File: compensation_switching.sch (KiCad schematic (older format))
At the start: 5 parts, among them U16 TMUX6111PWR

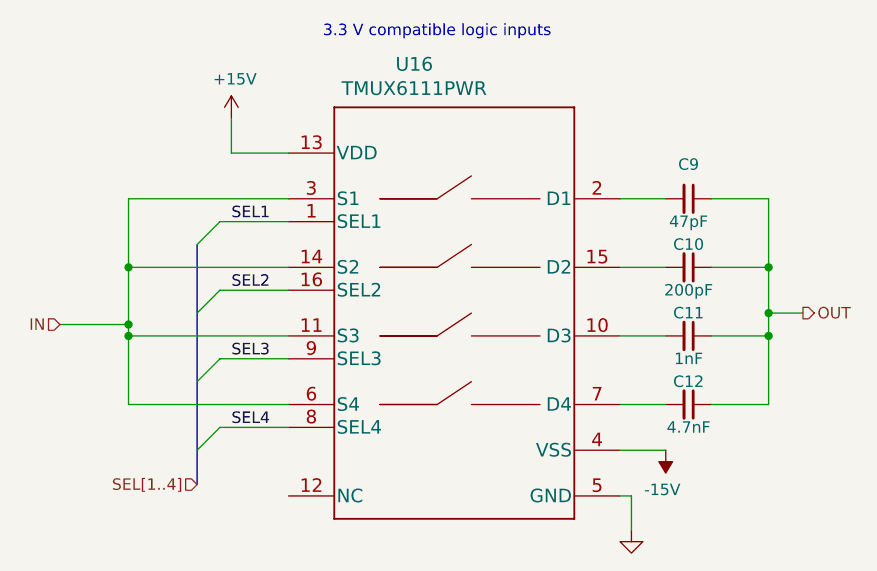
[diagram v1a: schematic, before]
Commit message: reduced ERC to just 4 warnings
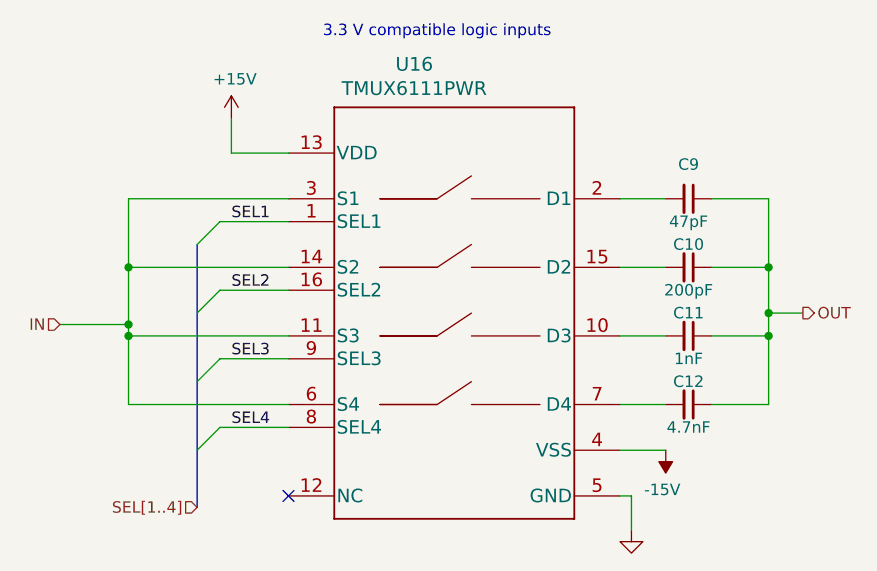
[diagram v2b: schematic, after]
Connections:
- no-connect marks 0 -> 1
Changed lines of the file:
@@
 $Descr A4 11693 8268
 encoding utf-8
-Sheet 3 6
+Sheet 6 6
 Title ""
 Date ""
@@
 AR Path="/6032F251/60DEADCD/60E82840" Ref="C?"  Part="1"
 AR Path="/6032F251/60DEBB32/60E82840" Ref="C?"  Part="1"
+AR Path="/6032F251/6217F546/60E82840" Ref="C9"  Part="1"
 F 0 "C9" V 6450 3300 50  0000 C CNN
 F 1 "47pF" V 6700 3300 50  0000 C CNN
@@
 AR Path="/6032F251/60DEADCD/60E839D5" Ref="C?"  Part="1"
 AR Path="/6032F251/60DEBB32/60E839D5" Ref="C?"  Part="1"
+AR Path="/6032F251/6217F546/60E839D5" Ref="C10"  Part="1"
 F 0 "C10" V 6500 3600 50  0000 C CNN
 F 1 "200pF" V 6700 3600 50  0000 C CNN
@@
 AR Path="/6032F251/60DEADCD/60E83CD7" Ref="C?"  Part="1"
 AR Path="/6032F251/60DEBB32/60E83CD7" Ref="C?"  Part="1"
+AR Path="/6032F251/6217F546/60E83CD7" Ref="C11"  Part="1"
 F 0 "C11" V 6500 3900 50  0000 C CNN
 F 1 "1nF" V 6700 3900 50  0000 C CNN
@@
 AR Path="/6032F251/60DEADCD/60E84E8C" Ref="C?"  Part="1"
 AR Path="/6032F251/60DEBB32/60E84E8C" Ref="C?"  Part="1"
+AR Path="/6032F251/6217F546/60E84E8C" Ref="C12"  Part="1"
 F 0 "C12" V 6500 4200 50  0000 C CNN
 F 1 "4.7nF" V 6700 4200 50  0000 C CNN
@@
 AR Path="/6032F251/60DEADCD/60EA6FEC" Ref="#PWR?"  Part="1"
 AR Path="/6032F251/60DEBB32/60EA6FEC" Ref="#PWR?"  Part="1"
+AR Path="/6032F251/6217F546/60EA6FEC" Ref="#PWR048"  Part="1"
 F 0 "#PWR048" H 6500 4500 50  0001 C CNN
 F 1 "-15V" H 6515 4573 50  0000 C CNN
@@
 AR Path="/6032F251/60DEADCD/60EA7501" Ref="#PWR?"  Part="1"
 AR Path="/6032F251/60DEBB32/60EA7501" Ref="#PWR?"  Part="1"
+AR Path="/6032F251/6217F546/60EA7501" Ref="#PWR046"  Part="1"
 F 0 "#PWR046" H 4600 2800 50  0001 C CNN
 F 1 "+15V" H 4615 3123 50  0000 C CNN
@@
 AR Path="/6032F251/60DEADCD/60EA8BF4" Ref="#PWR?"  Part="1"
 AR Path="/6032F251/60DEBB32/60EA8BF4" Ref="#PWR?"  Part="1"
+AR Path="/6032F251/6217F546/60EA8BF4" Ref="#PWR047"  Part="1"
 F 0 "#PWR047" H 6350 4500 50  0001 C CNN
 F 1 "GND" H 6355 4577 50  0001 C CNN
@@
 AR Path="/6032F251/60DEADCD/60E9BE9C" Ref="U?"  Part="1"
 AR Path="/6032F251/60DEBB32/60E9BE9C" Ref="U?"  Part="1"
+AR Path="/6032F251/6217F546/60E9BE9C" Ref="U16"  Part="1"
 F 0 "U16" H 5400 4888 60  0000 C CNN
 F 1 "TMUX6111PWR" H 5400 4782 60  0000 C CNN
@@
 	1    0    0    -1
 $EndComp
-Text HLabel 4450 4550 0    50   Input ~ 0
+Text HLabel 4450 4650 0    50   Input ~ 0
 SEL[1..4]
 Text HLabel 3850 3850 0    50   Input ~ 0
@@
 Connection ~ 4150 3850
 Connection ~ 6950 3800
+NoConn ~ 4850 4600
 Wire Bus Line
-	4450 3500 4450 4550
+	4450 3500 4450 4650
 $EndSCHEMATC

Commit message: updates to pcb layout
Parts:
- U16: footprint digikey-footprints:TSSOP-14_W4.4mm -> Package_SO:TSSOP-16_4.4x5mm_P0.65mm
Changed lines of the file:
@@
 F 0 "U16" H 5400 4888 60  0000 C CNN
 F 1 "TMUX6111PWR" H 5400 4782 60  0000 C CNN
-F 2 "digikey-footprints:TSSOP-14_W4.4mm" H 5400 3740 60  0001 C CNN
+F 2 "Package_SO:TSSOP-16_4.4x5mm_P0.65mm" H 5400 3740 60  0001 C CNN
 F 3 "" H 5400 3800 60  0001 C CNN
 F 4 "TMUX6111PWR" H 5400 3800 50  0001 C CNN "Manf#"

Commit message: updates to schematic for alternate part #s
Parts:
- C12: Alternative MPN CL10C332JB8NNNC -> (none); Alternative Manf# (none) -> CL10C332JB8NNNC
- U16: Alternate Manf# (none) -> TMUX6112PWR; Alternate2 Manf# (none) -> TMUX6113PWR
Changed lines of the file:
@@
 F 2 "Capacitor_SMD:C_0603_1608Metric" H 6638 4050 50  0001 C CNN
 F 3 "~" H 6600 4200 50  0001 C CNN
-F 4 "CL10C332JB8NNNC" H 6500 4200 50  0001 C CNN "Alternative MPN"
-F 5 "CC0603JRNPO9BN332" H 6500 4200 50  0001 C CNN "Manf#"
+F 4 "CC0603JRNPO9BN332" H 6500 4200 50  0001 C CNN "Manf#"
+F 5 "CL10C332JB8NNNC" H 6500 4200 50  0001 C CNN "Alternative Manf#"
 F 6 "5%" H 6500 4200 50  0001 C CNN "Tolerance"
 F 7 "50V" H 6500 4200 50  0001 C CNN "voltage"
@@
 F 3 "" H 5400 3800 60  0001 C CNN
 F 4 "TMUX6111PWR" H 5400 3800 50  0001 C CNN "Manf#"
+F 5 "TMUX6112PWR" H 5400 3800 50  0001 C CNN "Alternate Manf#"
+F 6 "TMUX6113PWR" H 5400 3800 50  0001 C CNN "Alternate2 Manf#"
 	1    5400 3800
 	1    0    0    -1

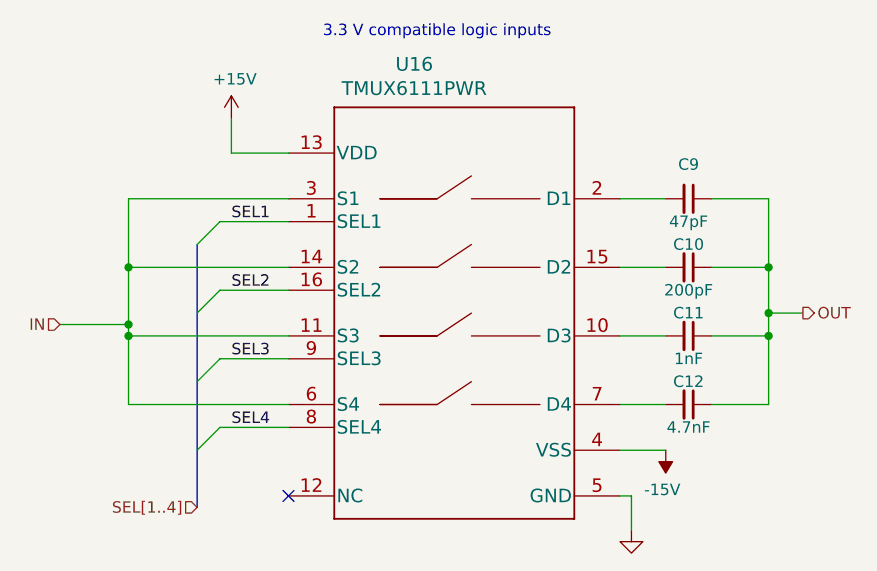
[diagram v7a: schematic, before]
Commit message: nearly completed layout re-route
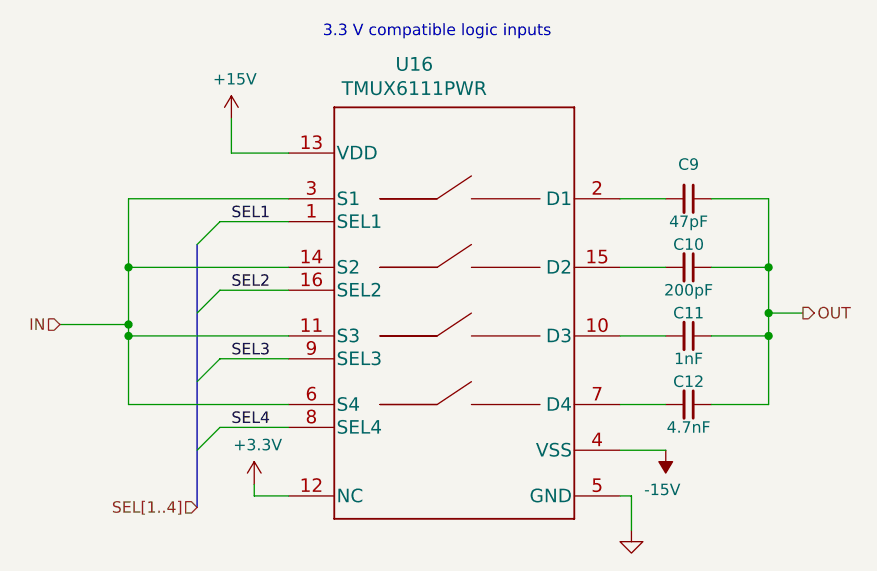
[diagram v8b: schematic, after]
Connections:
- net +3V3: now reaches U16.12 (NC)
- no-connect marks 1 -> 0
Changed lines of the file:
@@
 Connection ~ 4150 3850
 Connection ~ 6950 3800
-NoConn ~ 4850 4600
+$Comp
+L power:+3.3V #PWR?
+U 1 1 624F74AE
+P 4700 4550
+F 0 "#PWR?" H 4700 4400 50  0001 C CNN
+F 1 "+3.3V" H 4715 4723 50  0000 C CNN
+F 2 "" H 4700 4550 50  0001 C CNN
+F 3 "" H 4700 4550 50  0001 C CNN
+	1    4700 4550
+	1    0    0    -1
+$EndComp
+Wire Wire Line
+	4700 4550 4700 4600
+Wire Wire Line
+	4700 4600 4850 4600
 Wire Bus Line
 	4450 3500 4450 4650
